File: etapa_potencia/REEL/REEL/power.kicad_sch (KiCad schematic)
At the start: 23 parts, among them J5 USB_B_Mini, U1 Tp5400, U4 AMS1117-3.3

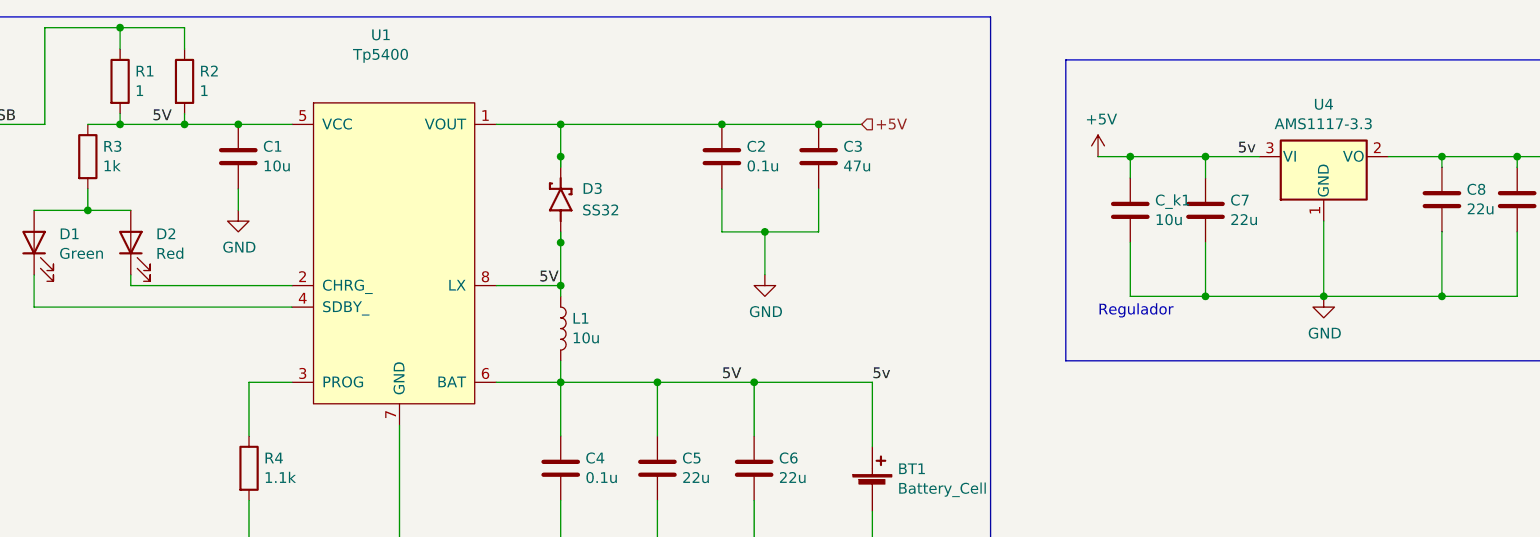
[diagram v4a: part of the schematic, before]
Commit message: Reorganización pcb
Después de primera revisión del profe Camargo
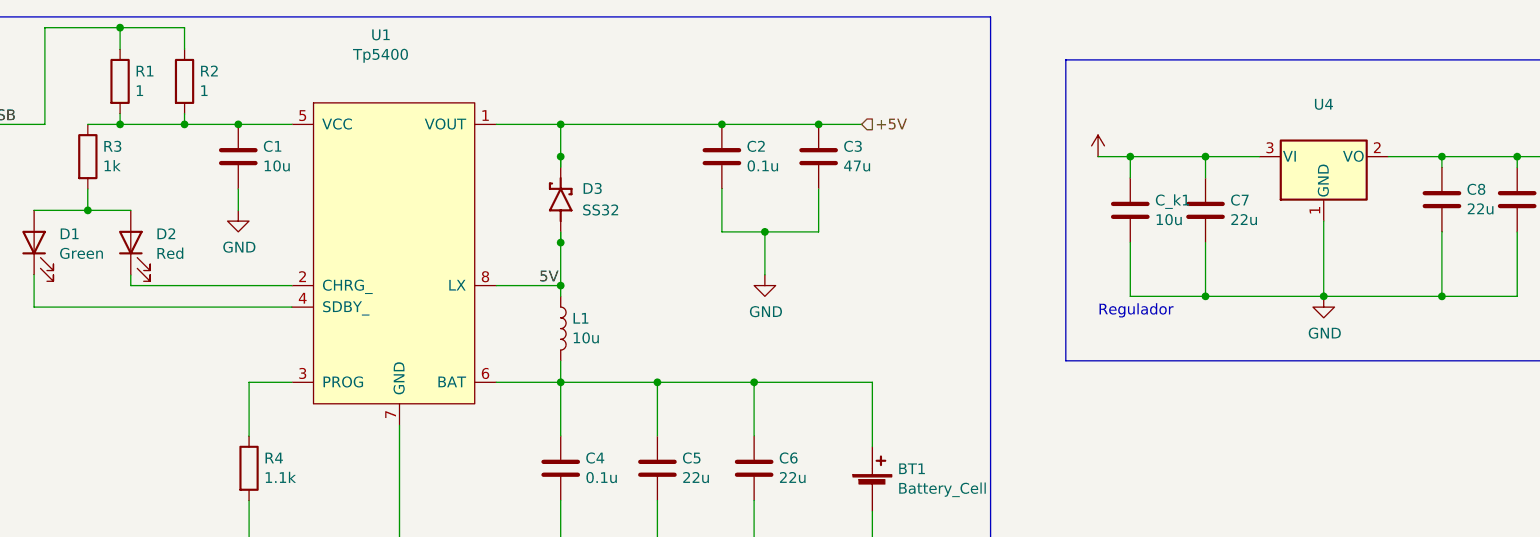
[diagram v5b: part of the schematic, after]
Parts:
- U4: value AMS1117-3.3 -> (none); footprint Package_TO_SOT_SMD:SOT-223-3_TabPin2 -> (none)
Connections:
- net +5V: no longer BT1.1 (+), C1.1, C4.1, C5.1, C6.1, D3.A, L1.1, L1.2, R1.2, R2.2, R3.1, U1.5 (VCC), U1.6 (BAT), U1.8 (LX)
- new net: BT1.1 (+), C4.1, C5.1, C6.1, L1.2, U1.6 (BAT)
- new net: C1.1, R1.2, R2.2, R3.1, U1.5 (VCC)
- new net 5V: D3.A, L1.1, U1.8 (LX)
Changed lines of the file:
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@@
-    (effects (font (size 1.27 1.27)) (justify left bottom))
-  )
-  (label "5v" (at 226.06 77.47 0)
     (effects (font (size 1.27 1.27)) (justify left bottom))
   )
@@
     (effects (font (size 1.27 1.27)) (justify left bottom))
   )
-  (label "5v" (at 182.88 104.14 0)
-    (effects (font (size 1.27 1.27)) (justify left bottom))
-  )
   (label "D+" (at 72.39 78.74 0)
-    (effects (font (size 1.27 1.27)) (justify left bottom))
-  )
-  (label "5V" (at 97.79 73.66 0)
-    (effects (font (size 1.27 1.27)) (justify left bottom))
-  )
-  (label "5V" (at 165.1 104.14 0)
     (effects (font (size 1.27 1.27)) (justify left bottom))
   )
@@
     (in_bom yes) (on_board yes)
     (property "Reference" "U4" (id 0) (at 236.22 71.3232 0))
-    (property "Value" "AMS1117-3.3" (id 1) (at 236.22 73.6346 0))
-    (property "Footprint" "Package_TO_SOT_SMD:SOT-223-3_TabPin2" (id 2) (at 236.22 72.39 0)
+    (property "Value" "" (id 1) (at 236.22 73.6346 0))
+    (property "Footprint" "" (id 2) (at 236.22 72.39 0)
       (effects (font (size 1.27 1.27)) hide)
     )
@@
       (effects (font (size 1.27 1.27)) hide)
     )
-    (property "Value" "+5V" (id 1) (at 209.931 73.0758 0))
+    (property "Value" "" (id 1) (at 209.931 73.0758 0))
     (property "Footprint" "" (id 2) (at 209.55 77.47 0)
       (effects (font (size 1.27 1.27)) hide)

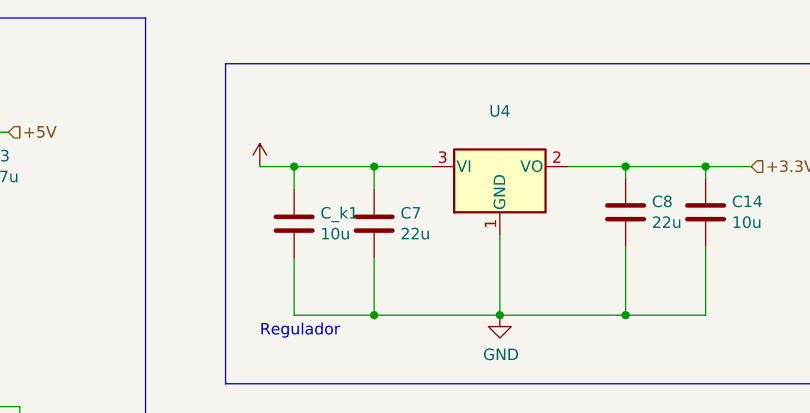
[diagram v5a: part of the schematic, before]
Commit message: Ordenar huellas en PCB ahora sí
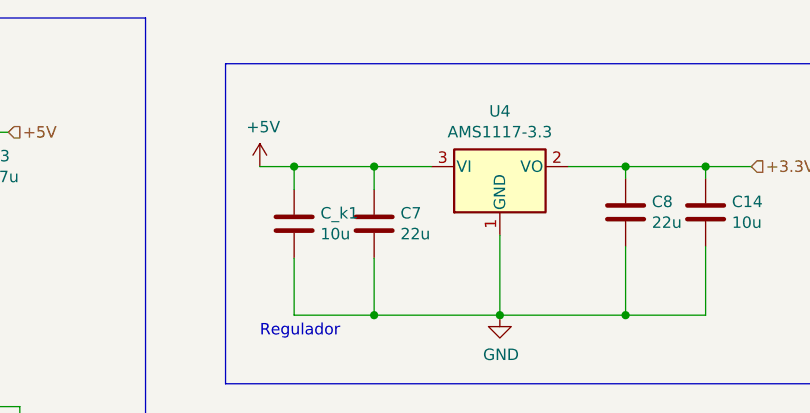
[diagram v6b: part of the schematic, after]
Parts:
- U4: value (none) -> AMS1117-3.3; footprint (none) -> Package_TO_SOT_SMD:SOT-223-3_TabPin2
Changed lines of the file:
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@@
     (in_bom yes) (on_board yes)
     (property "Reference" "U4" (id 0) (at 236.22 71.3232 0))
-    (property "Value" "" (id 1) (at 236.22 73.6346 0))
-    (property "Footprint" "" (id 2) (at 236.22 72.39 0)
+    (property "Value" "AMS1117-3.3" (id 1) (at 236.22 73.6346 0))
+    (property "Footprint" "Package_TO_SOT_SMD:SOT-223-3_TabPin2" (id 2) (at 236.22 72.39 0)
       (effects (font (size 1.27 1.27)) hide)
     )
@@
       (effects (font (size 1.27 1.27)) hide)
     )
-    (property "Value" "" (id 1) (at 209.931 73.0758 0))
+    (property "Value" "+5V" (id 1) (at 209.931 73.0758 0))
     (property "Footprint" "" (id 2) (at 209.55 77.47 0)
       (effects (font (size 1.27 1.27)) hide)
